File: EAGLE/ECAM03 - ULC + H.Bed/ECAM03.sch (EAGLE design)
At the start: 41 parts, among them J1 MODULAR TOOL, J2 FAN1, J3 FAN2, J4 FAN3, J5 S4B-PH-SM4, J6 SSR, J7 RINGLIGHT, Q2 16MHz, U1 SP3485, U2 ATMEGA238, U3 MCP4725, U4 MAX31855, U5 NTR4003NT3G, U6 NOR(74LVC), U8 AP3032

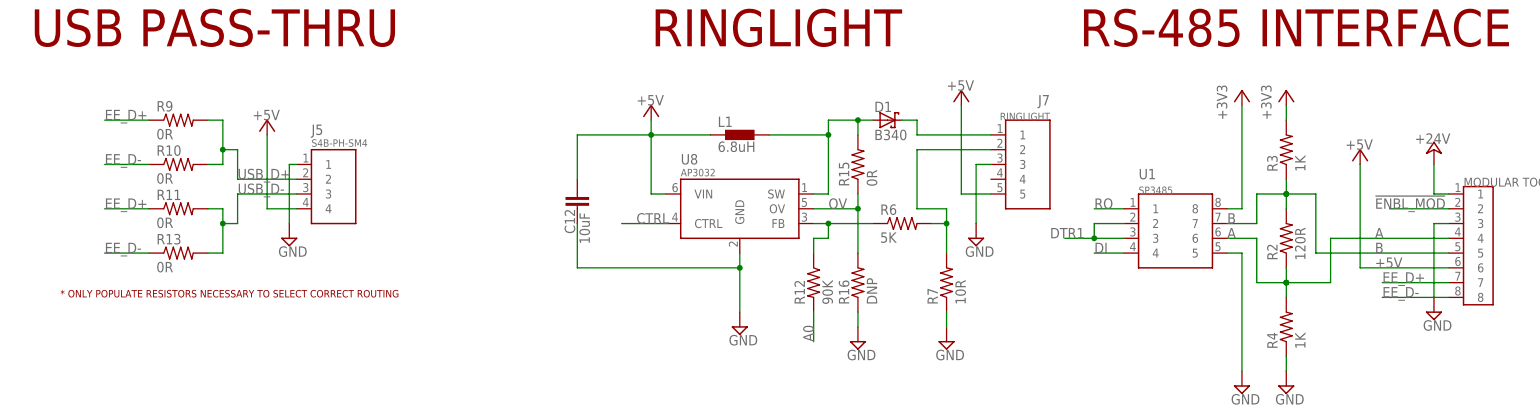
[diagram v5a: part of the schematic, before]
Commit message: Partially-routed diff pairs
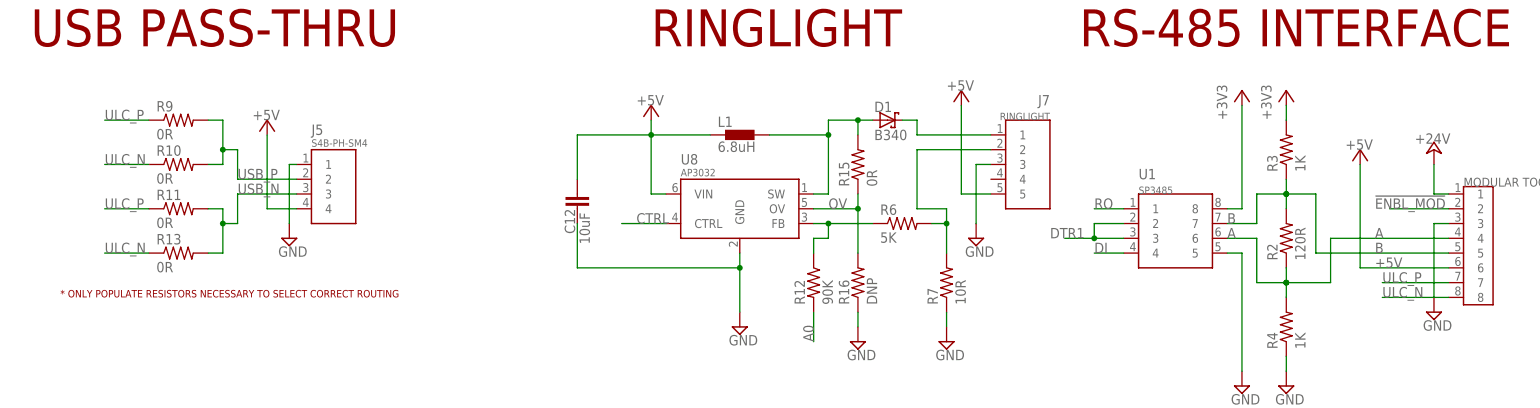
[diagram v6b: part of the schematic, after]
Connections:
- net EE_D+ renamed ULC_P
- net EE_D- renamed ULC_N
- net USB_D+ renamed USB_P
- net USB_D- renamed USB_N
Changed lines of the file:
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@@
-</segment>
-</net>
-<net name="EE_D+" class="0">
-<segment>
-<pinref part="J1" gate="G$1" pin="7"/>
-<wire x1="261.62" y1="109.22" x2="250.19" y2="109.22" width="0.1524" layer="91"/>
-<label x="250.19" y="109.22" size="1.778" layer="95"/>
-</segment>
-<segment>
-<wire x1="38.1" y1="137.16" x2="30.48" y2="137.16" width="0.1524" layer="91"/>
-<label x="30.48" y="137.16" size="1.778" layer="95" ratio="12"/>
-<pinref part="R9" gate="R$1" pin="1"/>
-</segment>
-<segment>
-<pinref part="R11" gate="R$1" pin="1"/>
-<wire x1="38.1" y1="121.92" x2="30.48" y2="121.92" width="0.1524" layer="91"/>
-<label x="30.48" y="121.92" size="1.778" layer="95" ratio="12"/>
-</segment>
-</net>
-<net name="EE_D-" class="0">
-<segment>
-<pinref part="J1" gate="G$1" pin="8"/>
-<wire x1="261.62" y1="106.68" x2="250.19" y2="106.68" width="0.1524" layer="91"/>
-<label x="250.19" y="106.68" size="1.778" layer="95"/>
-</segment>
-<segment>
-<wire x1="38.1" y1="114.3" x2="30.48" y2="114.3" width="0.1524" layer="91"/>
-<label x="30.48" y="114.3" size="1.778" layer="95" ratio="12"/>
-<pinref part="R13" gate="R$1" pin="1"/>
-</segment>
-<segment>
-<pinref part="R10" gate="R$1" pin="1"/>
-<wire x1="38.1" y1="129.54" x2="30.48" y2="129.54" width="0.1524" layer="91"/>
-<label x="30.48" y="129.54" size="1.778" layer="95" ratio="12"/>
 </segment>
 </net>
@@
 </segment>
 </net>
-<net name="USB_D+" class="0">
+<net name="USB_P" class="0">
 <segment>
 <pinref part="J5" gate="G$1" pin="2"/>
@@
 </segment>
 </net>
-<net name="USB_D-" class="0">
+<net name="USB_N" class="0">
 <segment>
 <pinref part="J5" gate="G$1" pin="3"/>
@@
 </segment>
 </net>
+<net name="ULC_P" class="0">
+<segment>
+<pinref part="J1" gate="G$1" pin="7"/>
+<wire x1="261.62" y1="109.22" x2="250.19" y2="109.22" width="0.1524" layer="91"/>
+<label x="250.19" y="109.22" size="1.778" layer="95"/>
+</segment>
+<segment>
+<wire x1="38.1" y1="137.16" x2="30.48" y2="137.16" width="0.1524" layer="91"/>
+<label x="30.48" y="137.16" size="1.778" layer="95" ratio="12"/>
+<pinref part="R9" gate="R$1" pin="1"/>
+</segment>
+<segment>
+<pinref part="R11" gate="R$1" pin="1"/>
+<wire x1="38.1" y1="121.92" x2="30.48" y2="121.92" width="0.1524" layer="91"/>
+<label x="30.48" y="121.92" size="1.778" layer="95" ratio="12"/>
+</segment>
+</net>
+<net name="ULC_N" class="0">
+<segment>
+<pinref part="J1" gate="G$1" pin="8"/>
+<wire x1="261.62" y1="106.68" x2="250.19" y2="106.68" width="0.1524" layer="91"/>
+<label x="250.19" y="106.68" size="1.778" layer="95"/>
+</segment>
+<segment>
+<pinref part="R10" gate="R$1" pin="1"/>
+<wire x1="38.1" y1="129.54" x2="30.48" y2="129.54" width="0.1524" layer="91"/>
+<label x="30.48" y="129.54" size="1.778" layer="95" ratio="12"/>
+</segment>
+<segment>
+<wire x1="38.1" y1="114.3" x2="30.48" y2="114.3" width="0.1524" layer="91"/>
+<label x="30.48" y="114.3" size="1.778" layer="95" ratio="12"/>
+<pinref part="R13" gate="R$1" pin="1"/>
+</segment>
+</net>

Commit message: Final(??) Versions of FPD boards.
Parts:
- added C6: 0.1uF, TinWhiskers:CPL-CAP-X7R-0603-100NF-50V
- added J8: FTDI, TinWhiskers:CPL-CON-HEADER-0.1IN-6P-M
- added J9: SPI, TinWhiskers:CPL-CON-HEADER-0.1IN-2X3P-M
- added R14: 10K, TinWhiskers:CPL-RES-0603-10K-0.1W
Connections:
- new net N$16: C6.1, J8.6
- net +5V: now also J8.3, J9.2, R14.2
- net DI: now also J8.5
- net GND: now also J8.1, J8.2, J9.6
- net MISO: now also J9.1
- net MOSI: now also J9.4
- net RESET: now also C6.2, J9.5, R14.1
- net RO: now also J8.4
- net SCK: now also J9.3
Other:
- note added: "FTDI INTERFACE"
- note added: "SPI"
- note added: "SPI INTERFACE"
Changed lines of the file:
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@@
 <part name="SUPPLY15" library="TinWhiskers" deviceset="GND" device=""/>
 <part name="P+13" library="supply1" deviceset="+5V" device=""/>
+<part name="J8" library="TinWhiskers" deviceset="CPL-CON-HEADER-0.1IN-6P-M" device="" value="FTDI">
+<attribute name="PARTNO" value="S6B-PH-SM4-TB(LF)(SN)"/>
+</part>
+<part name="SUPPLY17" library="TinWhiskers" deviceset="GND" device=""/>
+<part name="P+14" library="supply1" deviceset="+5V" device=""/>
+<part name="C6" library="TinWhiskers" deviceset="CPL-CAP-X7R-0603-100NF-50V" device="" value="0.1uF">
+<attribute name="PARTNO" value="UMK107B7104KA-T"/>
+</part>
+<part name="R14" library="TinWhiskers" deviceset="CPL-RES-0603-10K-0.1W" device="" value="10K">
+<attribute name="PARTNO" value="RC0603FR-0710KL"/>
+</part>
+<part name="J9" library="TinWhiskers" deviceset="CPL-CON-HEADER-0.1IN-2X3P-M" device="" value="SPI"/>
+<part name="P+15" library="supply1" deviceset="+5V" device=""/>
+<part name="P+16" library="supply1" deviceset="+5V" device=""/>
+<part name="SUPPLY18" library="TinWhiskers" deviceset="GND" device=""/>
 </parts>
 <sheets>
@@
 <text x="281.94" y="68.58" size="6.35" layer="94" ratio="10">SSR ENABLE</text>
 <text x="297.18" y="149.86" size="6.35" layer="94" ratio="10">V-REG (5V-3.3V)</text>
+<text x="12.7" y="218.44" size="6.35" layer="94" ratio="10">FTDI INTERFACE</text>
+<text x="99.06" y="218.44" size="6.35" layer="94" ratio="10">SPI INTERFACE</text>
+<text x="132.08" y="203.454" size="1.27" layer="96" ratio="10">SPI</text>
 </plain>
 <instances>
@@
 <instance part="P+13" gate="1" x="177.8" y="142.24" smashed="yes">
 <attribute name="VALUE" x="175.26" y="142.24" size="1.778" layer="96"/>
+</instance>
+<instance part="J8" gate="G$1" x="38.1" y="203.2" smashed="yes">
+<attribute name="NAME" x="33.02" y="213.36" size="1.778" layer="95" font="vector" ratio="12"/>
+<attribute name="VALUE" x="33.02" y="211.582" size="1.27" layer="96" font="vector" ratio="10"/>
+<attribute name="PARTNO" x="38.1" y="203.2" size="2.54" layer="96" ratio="10" display="off"/>
+</instance>
+<instance part="SUPPLY17" gate="GND" x="45.72" y="187.96" smashed="yes">
+<attribute name="VALUE" x="43.815" y="184.785" size="1.778" layer="96"/>
+</instance>
+<instance part="P+14" gate="1" x="48.26" y="213.36" smashed="yes">
+<attribute name="VALUE" x="45.72" y="213.36" size="1.778" layer="96"/>
+</instance>
+<instance part="C6" gate="C1" x="55.88" y="195.58" smashed="yes">
+<attribute name="NAME" x="49.784" y="195.961" size="1.778" layer="95"/>
+<attribute name="VALUE" x="47.244" y="193.421" size="1.778" layer="96"/>
+<attribute name="PARTNO" x="55.88" y="195.58" size="2.54" layer="96" ratio="10" display="off"/>
+</instance>
+<instance part="R14" gate="G$1" x="116.84" y="203.2" smashed="yes" rot="R90">
+<attribute name="NAME" x="115.3414" y="199.39" size="1.778" layer="95" rot="R90"/>
+<attribute name="VALUE" x="120.142" y="199.39" size="1.778" layer="96" rot="R90"/>
+<attribute name="PARTNO" x="116.84" y="203.2" size="2.54" layer="96" ratio="10" display="off"/>
+</instance>
+<instance part="J9" gate="G$1" x="134.62" y="200.66" smashed="yes" rot="R180">
+<attribute name="NAME" x="132.08" y="205.74" size="1.778" layer="125" ratio="12"/>
+</instance>
+<instance part="P+15" gate="1" x="116.84" y="213.36" smashed="yes">
+<attribute name="VALUE" x="114.3" y="213.36" size="1.778" layer="96"/>
+</instance>
+<instance part="P+16" gate="1" x="149.86" y="205.74" smashed="yes">
+<attribute name="VALUE" x="147.32" y="205.74" size="1.778" layer="96"/>
+</instance>
+<instance part="SUPPLY18" gate="GND" x="149.86" y="190.5" smashed="yes">
+<attribute name="VALUE" x="147.955" y="187.325" size="1.778" layer="96"/>
 </instance>
 </instances>
@@
 <wire x1="180.34" y1="129.54" x2="180.34" y2="119.38" width="0.1524" layer="91"/>
 </segment>
+<segment>
+<pinref part="J8" gate="G$1" pin="1"/>
+<wire x1="43.18" y1="208.28" x2="45.72" y2="208.28" width="0.1524" layer="91"/>
+<wire x1="45.72" y1="208.28" x2="45.72" y2="205.74" width="0.1524" layer="91"/>
+<pinref part="J8" gate="G$1" pin="2"/>
+<wire x1="45.72" y1="205.74" x2="45.72" y2="190.5" width="0.1524" layer="91"/>
+<wire x1="43.18" y1="205.74" x2="45.72" y2="205.74" width="0.1524" layer="91"/>
+<junction x="45.72" y="205.74"/>
+<pinref part="SUPPLY17" gate="GND" pin="GND"/>
+</segment>
+<segment>
+<pinref part="J9" gate="G$1" pin="6"/>
+<wire x1="147.32" y1="195.58" x2="149.86" y2="195.58" width="0.1524" layer="91"/>
+<wire x1="149.86" y1="195.58" x2="149.86" y2="193.04" width="0.1524" layer="91"/>
+<pinref part="SUPPLY18" gate="GND" pin="GND"/>
+</segment>
 </net>
 <net name="+5V" class="0">
@@
 <pinref part="P+13" gate="1" pin="+5V"/>
 </segment>
+<segment>
+<pinref part="J8" gate="G$1" pin="3"/>
+<wire x1="43.18" y1="203.2" x2="48.26" y2="203.2" width="0.1524" layer="91"/>
+<wire x1="48.26" y1="203.2" x2="48.26" y2="210.82" width="0.1524" layer="91"/>
+<pinref part="P+14" gate="1" pin="+5V"/>
+</segment>
+<segment>
+<pinref part="R14" gate="G$1" pin="2"/>
+<pinref part="P+15" gate="1" pin="+5V"/>
+<wire x1="116.84" y1="208.28" x2="116.84" y2="210.82" width="0.1524" layer="91"/>
+</segment>
+<segment>
+<pinref part="J9" gate="G$1" pin="2"/>
+<wire x1="147.32" y1="200.66" x2="149.86" y2="200.66" width="0.1524" layer="91"/>
+<wire x1="149.86" y1="200.66" x2="149.86" y2="203.2" width="0.1524" layer="91"/>
+<pinref part="P+16" gate="1" pin="+5V"/>
+</segment>
 </net>
 <net name="RO" class="0">
@@
 <label x="200.66" y="121.92" size="1.778" layer="95" ratio="12"/>
 </segment>
+<segment>
+<pinref part="J8" gate="G$1" pin="4"/>
+<wire x1="43.18" y1="200.66" x2="50.8" y2="200.66" width="0.1524" layer="91"/>
+<label x="48.26" y="200.66" size="1.778" layer="95" ratio="12"/>
+</segment>
 </net>
 <net name="DI" class="0">
@@
 <label x="200.66" y="114.3" size="1.778" layer="95" ratio="12"/>
 </segment>
+<segment>
+<pinref part="J8" gate="G$1" pin="5"/>
+<wire x1="43.18" y1="198.12" x2="50.8" y2="198.12" width="0.1524" layer="91"/>
+<label x="48.26" y="198.12" size="1.778" layer="95" ratio="12"/>
+</segment>
 </net>
 <net name="SSR" class="0">
@@
 <label x="180.34" y="50.8" size="1.778" layer="95"/>
 </segment>
+<segment>
+<pinref part="J9" gate="G$1" pin="3"/>
+<wire x1="129.54" y1="198.12" x2="121.92" y2="198.12" width="0.1524" layer="91"/>
+<label x="121.92" y="198.12" size="1.778" layer="95" ratio="10"/>
+</segment>
 </net>
 <net name="MOSI" class="0">
@@
 <label x="312.42" y="223.52" size="1.778" layer="95" ratio="12"/>
 </segment>
+<segment>
+<pinref part="J9" gate="G$1" pin="4"/>
+<wire x1="147.32" y1="198.12" x2="154.94" y2="198.12" width="0.1524" layer="91"/>
+<label x="147.32" y="198.12" size="1.778" layer="95" ratio="10"/>
+</segment>
 </net>
 <net name="RESET" class="0">
@@
 <wire x1="322.58" y1="193.04" x2="312.42" y2="193.04" width="0.1524" layer="91"/>
 <label x="312.42" y="193.04" size="1.778" layer="95" ratio="12"/>
+</segment>
+<segment>
+<pinref part="C6" gate="C1" pin="2"/>
+<wire x1="58.42" y1="195.58" x2="60.96" y2="195.58" width="0.1524" layer="91"/>
+<label x="58.42" y="195.58" size="1.778" layer="95" ratio="12"/>
+</segment>
+<segment>
+<pinref part="J9" gate="G$1" pin="5"/>
+<wire x1="129.54" y1="195.58" x2="116.84" y2="195.58" width="0.1524" layer="91"/>
+<wire x1="116.84" y1="195.58" x2="116.84" y2="198.12" width="0.1524" layer="91"/>
+<label x="121.92" y="195.58" size="1.778" layer="95" ratio="10"/>
+<pinref part="R14" gate="G$1" pin="1"/>
 </segment>
 </net>
@@
 <label x="180.34" y="55.88" size="1.778" layer="95"/>
 </segment>
+<segment>
+<pinref part="J9" gate="G$1" pin="1"/>
+<wire x1="129.54" y1="200.66" x2="121.92" y2="200.66" width="0.1524" layer="91"/>
+<label x="121.92" y="200.66" size="1.778" layer="95" ratio="10"/>
+</segment>
 </net>
 <net name="SCL" class="0">
@@
 </segment>
 </net>
+<net name="N$16" class="0">
+<segment>
+<pinref part="J8" gate="G$1" pin="6"/>
+<wire x1="43.18" y1="195.58" x2="50.8" y2="195.58" width="0.1524" layer="91"/>
+<pinref part="C6" gate="C1" pin="1"/>
+</segment>
+</net>
